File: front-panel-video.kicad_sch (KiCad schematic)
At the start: 23 parts, among them J6 DisplayPort-Mini_TE_2129320-3, U11 TPD4E05U06QDQARQ1, U12 TPD4E05U06QDQARQ1, U13 TPD4E05U06QDQARQ1

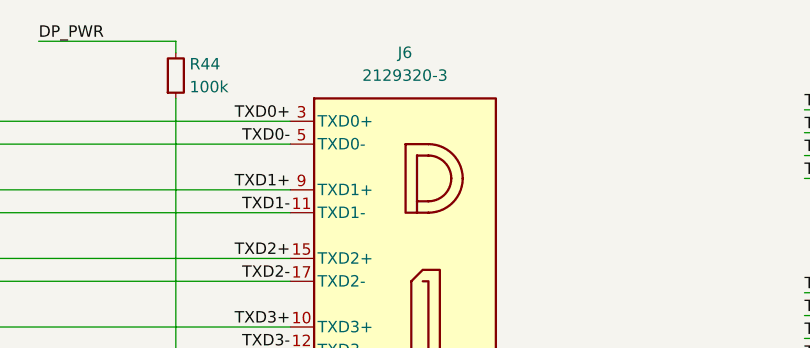
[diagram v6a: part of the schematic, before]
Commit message: Replace Mini DP connector with E9320-001-01
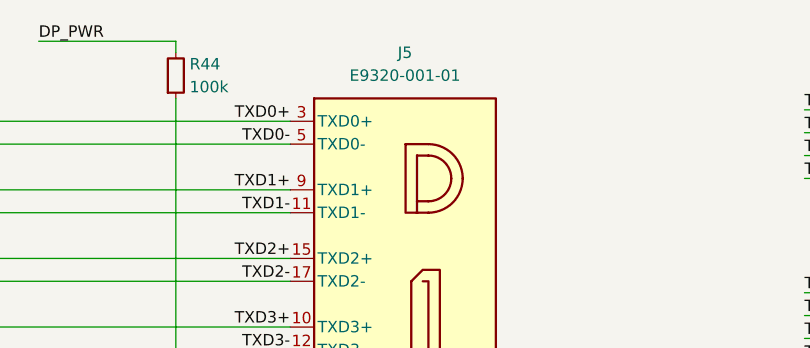
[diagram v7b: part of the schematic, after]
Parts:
- removed J6: DisplayPort-Mini_TE_2129320-3, antmicro-footprints:DisplayPort-Mini_Receptacle_TE_2129320-3, symbol antmicroVideoConnectors:DisplayPort-Mini_TE_2129320-3
- added J5: DisplayPort-Mini_Pulse_E9320-001-01, antmicro-footprints:DisplayPort-Mini_Receptacle_Pulse_E9320-001-01, symbol antmicroVideoConnectors:DisplayPort-Mini_PulseElectronics_E9320-001-01
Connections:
- net AUX+: now also J5.16 (AUX+)
- net AUX-: now also J5.18 (AUX-)
- net CFG1: now also J5.4 (CFG1)
- net CFG2: now also J5.6 (CFG2)
- net DP_PWR: now also J5.20 (DP_PWR)
- net GND: now also J5.1 (GND), J5.13 (GND), J5.14 (GND), J5.19 (GND), J5.7 (GND), J5.8 (GND), J5.SH
- net HPD: now also J5.2 (HPD)
- net TXD0+: now also J5.3 (TXD0+)
- net TXD0-: now also J5.5 (TXD0-)
- net TXD1+: now also J5.9 (TXD1+)
- net TXD1-: now also J5.11 (TXD1-)
- net TXD2+: now also J5.15 (TXD2+)
- net TXD2-: now also J5.17 (TXD2-)
- net TXD3+: now also J5.10 (TXD3+)
- net TXD3-: now also J5.12 (TXD3-)
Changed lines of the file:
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@@
-	)
-	(symbol
-		(lib_id "antmicroVideoConnectors:DisplayPort-Mini_TE_2129320-3")
-		(at 204.47 107.95 0)
-		(unit 1)
-		(exclude_from_sim no)
-		(in_bom yes)
-		(on_board yes)
-		(dnp no)
-		(fields_autoplaced yes)
-		(property "Reference" "J6"
-			(at 217.2335 100.33 0)
-			(effects
-				(font
-					(size 1.27 1.27)
-					(thickness 0.15)
-				)
-			)
-		)
-		(property "Value" "DisplayPort-Mini_TE_2129320-3"
-			(at 250.19 107.95 0)
-			(effects
-				(font
-					(size 1.27 1.27)
-					(thickness 0.15)
-				)
-				(justify left bottom)
-				(hide yes)
-			)
-		)
-		(property "Footprint" "antmicro-footprints:DisplayPort-Mini_Receptacle_TE_2129320-3"
-			(at 250.19 110.49 0)
-			(effects
-				(font
-					(size 1.27 1.27)
-					(thickness 0.15)
-				)
-				(justify left bottom)
-				(hide yes)
-			)
-		)
-		(property "Datasheet" "https://www.te.com/usa-en/product-2129320-3.html"
-			(at 250.19 113.03 0)
-			(effects
-				(font
-					(size 1.27 1.27)
-					(thickness 0.15)
-				)
-				(justify left bottom)
-				(hide yes)
-			)
-		)
-		(property "Description" "DisplayPort, Mini Receptacle Connector 20 Position Through Hole, Right Angle"
-			(at 204.47 107.95 0)
-			(effects
-				(font
-					(size 1.27 1.27)
-				)
-				(hide yes)
-			)
-		)
-		(property "MPN" "2129320-3"
-			(at 217.2335 102.87 0)
-			(effects
-				(font
-					(size 1.27 1.27)
-					(thickness 0.15)
-				)
-			)
-		)
-		(property "Manufacturer" "TE Connectivity"
-			(at 250.19 118.11 0)
-			(effects
-				(font
-					(size 1.27 1.27)
-					(thickness 0.15)
-				)
-				(justify left bottom)
-				(hide yes)
-			)
-		)
-		(property "Author" "Antmicro"
-			(at 250.19 120.65 0)
-			(effects
-				(font
-					(size 1.27 1.27)
-					(thickness 0.15)
-				)
-				(justify left bottom)
-				(hide yes)
-			)
-		)
-		(property "License" "Apache-2.0"
-			(at 250.19 123.19 0)
-			(effects
-				(font
-					(size 1.27 1.27)
-					(thickness 0.15)
-				)
-				(justify left bottom)
-				(hide yes)
-			)
-		)
-		(pin "5"
-		)
-		(pin "SH"
-		)
-		(pin "8"
-		)
-		(pin "13"
-		)
-		(pin "19"
-		)
-		(pin "16"
-		)
-		(pin "20"
-		)
-		(pin "15"
-		)
-		(pin "6"
-		)
-		(pin "1"
-		)
-		(pin "11"
-		)
-		(pin "7"
-		)
-		(pin "17"
-		)
-		(pin "14"
-		)
-		(pin "4"
-		)
-		(pin "10"
-		)
-		(pin "2"
-		)
-		(pin "9"
-		)
-		(pin "12"
-		)
-		(pin "18"
-		)
-		(pin "3"
-		)
-		(instances
-			(project ""
-				(path "/5f636c45-3c15-4731-8931-4625e0dab7e4/32de8c9e-be2b-4d78-9d5d-f4e694f2d2e7"
-					(reference "J6")
-					(unit 1)
-				)
-			)
-		)
 	)
 	(symbol
@@
 					(unit 1)
 				)
+			)
+		)
+	)
+	(symbol
+		(lib_id "antmicroVideoConnectors:DisplayPort-Mini_PulseElectronics_E9320-001-01")
+		(at 204.47 107.95 0)
+		(unit 1)
+		(exclude_from_sim no)
+		(in_bom yes)
+		(on_board yes)
+		(dnp no)
+		(fields_autoplaced yes)
+		(property "Reference" "J5"
+			(at 217.2335 100.33 0)
+			(effects
+				(font
+					(size 1.27 1.27)
+					(thickness 0.15)
+				)
+			)
+		)
+		(property "Value" "DisplayPort-Mini_Pulse_E9320-001-01"
+			(at 250.19 107.95 0)
+			(effects
+				(font
+					(size 1.27 1.27)
+					(thickness 0.15)
+				)
+				(justify left bottom)
+				(hide yes)
+			)
+		)
+		(property "Footprint" "antmicro-footprints:DisplayPort-Mini_Receptacle_Pulse_E9320-001-01"
+			(at 250.19 110.49 0)
+			(effects
+				(font
+					(size 1.27 1.27)
+					(thickness 0.15)
+				)
+				(justify left bottom)
+				(hide yes)
+			)
+		)
+		(property "Datasheet" "https://mm.digikey.com/Volume0/opasdata/d220001/medias/docus/6167/E9320-001-0x.pdf"
+			(at 250.19 113.03 0)
+			(effects
+				(font
+					(size 1.27 1.27)
+					(thickness 0.15)
+				)
+				(justify left bottom)
+				(hide yes)
+			)
+		)
+		(property "Description" "DisplayPort, Mini Receptacle Connector 20 Position THT/SMD, Right Angle"
+			(at 204.47 107.95 0)
+			(effects
+				(font
+					(size 1.27 1.27)
+				)
+				(hide yes)
+			)
+		)
+		(property "MPN" "E9320-001-01"
+			(at 217.2335 102.87 0)
+			(effects
+				(font
+					(size 1.27 1.27)
+					(thickness 0.15)
+				)
+			)
+		)
+		(property "Manufacturer" " Pulse Electronics"
+			(at 250.19 118.11 0)
+			(effects
+				(font
+					(size 1.27 1.27)
+					(thickness 0.15)
+				)
+				(justify left bottom)
+				(hide yes)
+			)
+		)
+		(property "Author" "Antmicro"
+			(at 250.19 120.65 0)
+			(effects
+				(font
+					(size 1.27 1.27)
+					(thickness 0.15)
+				)
+				(justify left bottom)
+				(hide yes)
+			)
+		)
+		(property "License" "Apache-2.0"
+			(at 250.19 123.19 0)
+			(effects
+				(font
+					(size 1.27 1.27)
+					(thickness 0.15)
+				)
+				(justify left bottom)
+				(hide yes)
+			)
+		)
+		(pin "16"
+		)
+		(pin "11"
+		)
+		(pin "14"
+		)
+		(pin "17"
+		)
+		(pin "6"
+		)
+		(pin "SH"
+		)
+		(pin "5"
+		)
+		(pin "4"
+		)
+		(pin "12"
+		)
+		(pin "10"
+		)
+		(pin "13"
+		)
+		(pin "20"
+		)
+		(pin "1"
+		)
+		(pin "15"
+		)
+		(pin "18"
+		)
+		(pin "3"
+		)
+		(pin "19"
+		)
+		(pin "8"
+		)
+		(pin "2"
+		)
+		(pin "9"
+		)
+		(pin "7"
+		)
+		(instances
+			(project ""
+				(path "/5f636c45-3c15-4731-8931-4625e0dab7e4/32de8c9e-be2b-4d78-9d5d-f4e694f2d2e7"
+					(reference "J5")
+					(unit 1)
+				)

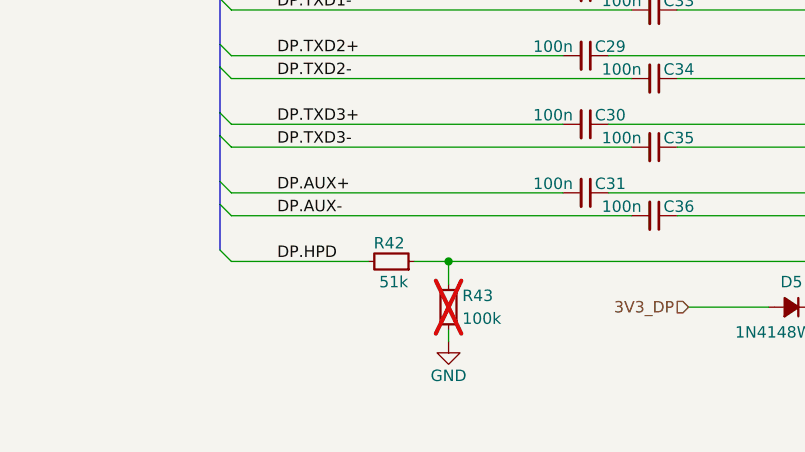
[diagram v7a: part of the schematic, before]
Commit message: [#83363] Adjusted HPD connection
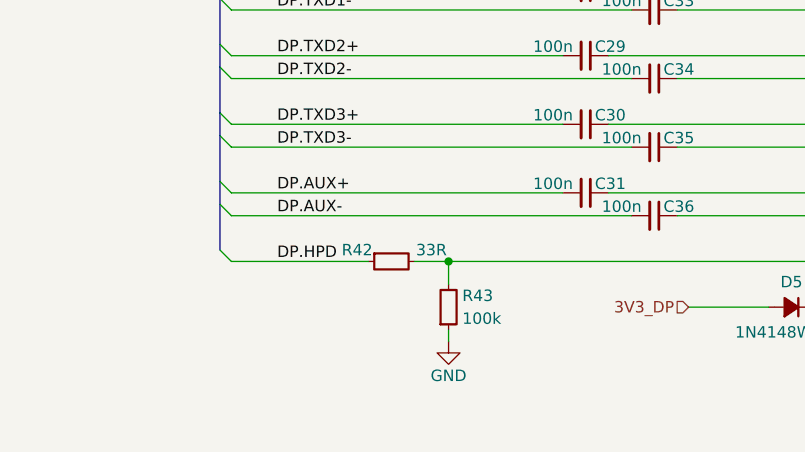
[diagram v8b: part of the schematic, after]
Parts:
- removed R42: R_51k_0402, antmicro-footprints:R_0402_1005Metric, symbol antmicroResistors0402:R_51k_0402
- added R42: R_33R_0402, antmicro-footprints:R_0402_1005Metric, symbol antmicroResistors0402:R_33R_0402
- R43: now fitted
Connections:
- net DP.HPD: now also R42.1
- net HPD: now also R42.2
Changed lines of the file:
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@@
-	)
-	(symbol
-		(lib_id "antmicroResistors0402:R_51k_0402")
-		(at 123.19 146.05 180)
-		(unit 1)
-		(exclude_from_sim no)
-		(in_bom yes)
-		(on_board yes)
-		(dnp no)
-		(property "Reference" "R42"
-			(at 120.396 144.018 0)
-			(effects
-				(font
-					(size 1.27 1.27)
-					(thickness 0.15)
-				)
-			)
-		)
-		(property "Value" "R_51k_0402"
-			(at 102.87 133.35 0)
-			(effects
-				(font
-					(size 1.27 1.27)
-					(thickness 0.15)
-				)
-				(justify left bottom)
-				(hide yes)
-			)
-		)
-		(property "Footprint" "antmicro-footprints:R_0402_1005Metric"
-			(at 102.87 130.81 0)
-			(effects
-				(font
-					(size 1.27 1.27)
-					(thickness 0.15)
-				)
-				(justify left bottom)
-				(hide yes)
-			)
-		)
-		(property "Datasheet" "https://www.bourns.com/docs/product-datasheets/cr.pdf"
-			(at 102.87 128.27 0)
-			(effects
-				(font
-					(size 1.27 1.27)
-					(thickness 0.15)
-				)
-				(justify left bottom)
-				(hide yes)
-			)
-		)
-		(property "Description" "SMD Chip Resistor, 51 kohm, ± 1%, 63 mW, 0402 [1005 Metric], Thick Film, General Purpose"
-			(at 123.19 146.05 0)
-			(effects
-				(font
-					(size 1.27 1.27)
-				)
-				(hide yes)
-			)
-		)
-		(property "MPN" "CR0402-FX-5102GLF"
-			(at 102.87 125.73 0)
-			(effects
-				(font
-					(size 1.27 1.27)
-					(thickness 0.15)
-				)
-				(justify left bottom)
-				(hide yes)
-			)
-		)
-		(property "Manufacturer" "Bourns"
-			(at 102.87 123.19 0)
-			(effects
-				(font
-					(size 1.27 1.27)
-					(thickness 0.15)
-				)
-				(justify left bottom)
-				(hide yes)
-			)
-		)
-		(property "License" "Apache-2.0"
-			(at 102.87 120.65 0)
-			(effects
-				(font
-					(size 1.27 1.27)
-					(thickness 0.15)
-				)
-				(justify left bottom)
-				(hide yes)
-			)
-		)
-		(property "Author" "Antmicro"
-			(at 102.87 118.11 0)
-			(effects
-				(font
-					(size 1.27 1.27)
-					(thickness 0.15)
-				)
-				(justify left bottom)
-				(hide yes)
-			)
-		)
-		(property "Val" "51k"
-			(at 120.904 148.336 0)
-			(effects
-				(font
-					(size 1.27 1.27)
-					(thickness 0.15)
-				)
-			)
-		)
-		(property "Tolerance" "1%"
-			(at 102.87 135.89 0)
-			(effects
-				(font
-					(size 1.27 1.27)
-				)
-				(justify left bottom)
-				(hide yes)
-			)
-		)
-		(pin "2"
-		)
-		(pin "1"
-		)
-		(instances
-			(project ""
-				(path "/5f636c45-3c15-4731-8931-4625e0dab7e4/32de8c9e-be2b-4d78-9d5d-f4e694f2d2e7"
-					(reference "R42")
-					(unit 1)
-				)
-			)
-		)
 	)
 	(symbol
@@
 	)
 	(symbol
+		(lib_id "antmicroResistors0402:R_33R_0402")
+		(at 118.11 146.05 0)
+		(unit 1)
+		(exclude_from_sim no)
+		(in_bom yes)
+		(on_board yes)
+		(dnp no)
+		(property "Reference" "R42"
+			(at 116.84 144.78 0)
+			(effects
+				(font
+					(size 1.27 1.27)
+					(thickness 0.15)
+				)
+			)
+		)
+		(property "Value" "R_33R_0402"
+			(at 138.43 158.75 0)
+			(effects
+				(font
+					(size 1.27 1.27)
+					(thickness 0.15)
+				)
+				(justify left bottom)
+				(hide yes)
+			)
+		)
+		(property "Footprint" "antmicro-footprints:R_0402_1005Metric"
+			(at 138.43 161.29 0)
+			(effects
+				(font
+					(size 1.27 1.27)
+					(thickness 0.15)
+				)
+				(justify left bottom)
+				(hide yes)
+			)
+		)
+		(property "Datasheet" "https://www.bourns.com/docs/product-datasheets/cr.pdf"
+			(at 138.43 163.83 0)
+			(effects
+				(font
+					(size 1.27 1.27)
+					(thickness 0.15)
+				)
+				(justify left bottom)
+				(hide yes)
+			)
+		)
+		(property "Description" "SMD Chip Resistor, 33 ohm, ± 1%, 62.5 mW, 0402 [1005 Metric], Thick Film, General Purpose"
+			(at 118.11 146.05 0)
+			(effects
+				(font
+					(size 1.27 1.27)
+				)
+				(hide yes)
+			)
+		)
+		(property "MPN" "CR0402-FX-33R0GLF"
+			(at 138.43 166.37 0)
+			(effects
+				(font
+					(size 1.27 1.27)
+					(thickness 0.15)
+				)
+				(justify left bottom)
+				(hide yes)
+			)
+		)
+		(property "Manufacturer" "Bourns"
+			(at 138.43 168.91 0)
+			(effects
+				(font
+					(size 1.27 1.27)
+					(thickness 0.15)
+				)
+				(justify left bottom)
+				(hide yes)
+			)
+		)
+		(property "License" "Apache-2.0"
+			(at 138.43 171.45 0)
+			(effects
+				(font
+					(size 1.27 1.27)
+					(thickness 0.15)
+				)
+				(justify left bottom)
+				(hide yes)
+			)
+		)
+		(property "Author" "Antmicro"
+			(at 138.43 173.99 0)
+			(effects
+				(font
+					(size 1.27 1.27)
+					(thickness 0.15)
+				)
+				(justify left bottom)
+				(hide yes)
+			)
+		)
+		(property "Val" "33R"
+			(at 125.095 144.78 0)
+			(effects
+				(font
+					(size 1.27 1.27)
+					(thickness 0.15)
+				)
+			)
+		)
+		(property "Tolerance" "1%"
+			(at 138.43 156.21 0)
+			(effects
+				(font
+					(size 1.27 1.27)
+				)
+				(justify left bottom)
+				(hide yes)
+			)
+		)
+		(pin "1"
+		)
+		(pin "2"
+		)
+		(instances
+			(project ""
+				(path "/5f636c45-3c15-4731-8931-4625e0dab7e4/32de8c9e-be2b-4d78-9d5d-f4e694f2d2e7"
+					(reference "R42")
+					(unit 1)
+				)
+			)
+		)
+	)
+	(symbol
 		(lib_id "antmicropower:GND")
 		(at 194.31 160.02 0)
@@
 		(in_bom no)
 		(on_board yes)
-		(dnp yes)
+		(dnp no)
 		(property "Reference" "R43"
 			(at 128.524 149.86 90)
